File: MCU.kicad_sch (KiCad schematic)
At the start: 2 parts, among them U3 STM32L476RGTx, U4 ESP-12F

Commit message: Updates
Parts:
- added C10, C8, C9: 10u, Capacitor_SMD:C_0603_1608Metric_Pad1.08x0.95mm_HandSolder, symbol Device:C
- added C11: 10n, Capacitor_SMD:C_0603_1608Metric_Pad1.08x0.95mm_HandSolder, symbol Device:C
- added C12, C13: 1u, Capacitor_SMD:C_0603_1608Metric_Pad1.08x0.95mm_HandSolder, symbol Device:C
- added FB1: 120R, Inductor_SMD:L_0603_1608Metric_Pad1.05x0.95mm_HandSolder, symbol Device:FerriteBead
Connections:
- net +3.3V: now reaches U3.1 (VBAT)
- net +3.3V: now also U3.19 (VDD), U3.32 (VDD), U3.48 (VDDUSB), U3.64 (VDD), U4.8 (VCC), C10.1, C13.1, C8.1, C9.1, FB1.2
- net GND: now reaches U3.12 (VSSA)
- net GND: now also U3.18 (VSS), U3.31 (VSS), U3.47 (VSS), U3.63 (VSS), U4.15 (GND), C10.2, C11.2, C12.2, C13.2, C8.2, C9.2
- net +3.3VA: now reaches U3.13 (VDDA)
- net +3.3VA: now also C11.1, C12.1, FB1.1
- net ESP_RST: now reaches U4.1 (~{RST})
- net ESP_RXD: now reaches U4.21 (GPIO3/RXD)
- net ESP_TXD: now reaches U4.22 (GPIO1/TXD)
- net ESP_EN: now reaches U4.3 (EN)
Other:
- moved on the sheet: U3, U4

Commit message: Clock
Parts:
- added C14, C15, C16: 10u, Capacitor_SMD:C_0603_1608Metric_Pad1.08x0.95mm_HandSolder, symbol Device:C
- added R2: 10k, Resistor_SMD:R_0603_1608Metric_Pad0.98x0.95mm_HandSolder, symbol Device:R
- added Y1: 16MHz, Crystal:Crystal_SMD_3225-4Pin_3.2x2.5mm_HandSoldering, symbol Device:Crystal_GND24
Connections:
- net GND: now also C14.2, C15.2, C16.2, R2.1, Y1.2, Y1.4
- net CLK_IN: now reaches U3.5 (PH0)
- net CLK_IN: now also C15.1, Y1.1
- net CLK_OUT: now reaches U3.6 (PH1)
- net CLK_OUT: now also C16.1, Y1.3
- net at U3.60 (BOOT0): now also R2.2
- net at U3.7 (NRST): now also C14.1
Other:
- moved on the sheet: C10, C11, C12, C13, C8, C9, FB1

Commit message: uPDATE
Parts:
- added J2: SWD, Connector_PinHeader_1.00mm:PinHeader_1x03_P1.00mm_Vertical, symbol Connector_Generic:Conn_01x03
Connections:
- net ESP_EN: now also U3.3 (PC14)
- net ESP_RST: now also U3.4 (PC15)
- net ESP_RXD: now also U3.51 (PC10)
- net ESP_TXD: now also U3.52 (PC11)
- net GND: now also U4.18 (GPIO0), J2.1 (Pin_1)
- net SWDIO: now reaches U3.46 (PA13)
- net SWDIO: now also J2.2 (Pin_2)
- net SWDCLK: now reaches U3.49 (PA14)
- net SWDCLK: now also J2.3 (Pin_3)

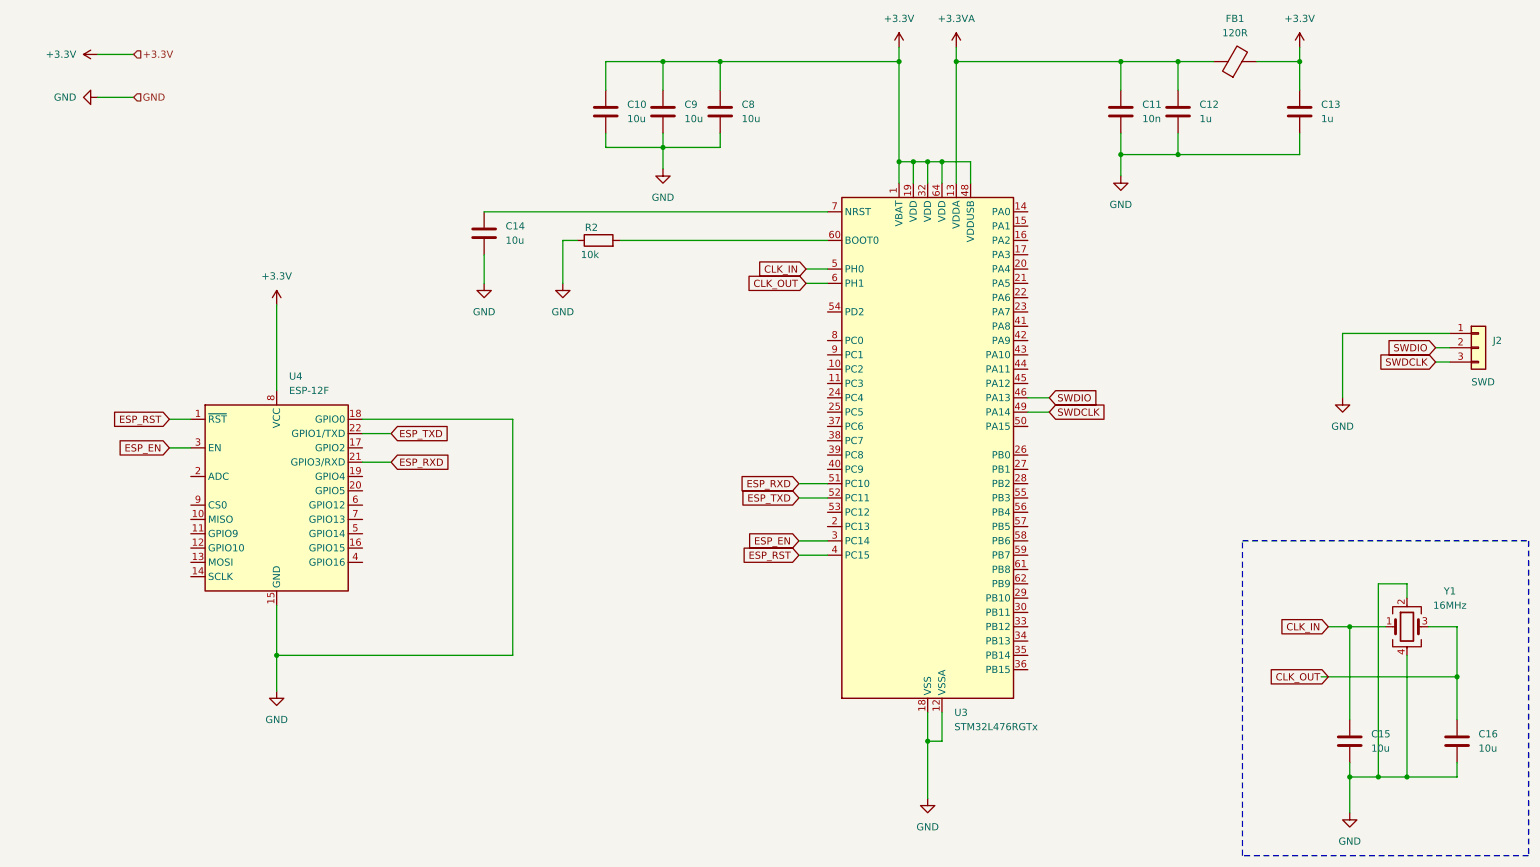
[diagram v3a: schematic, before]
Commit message: Schematic done
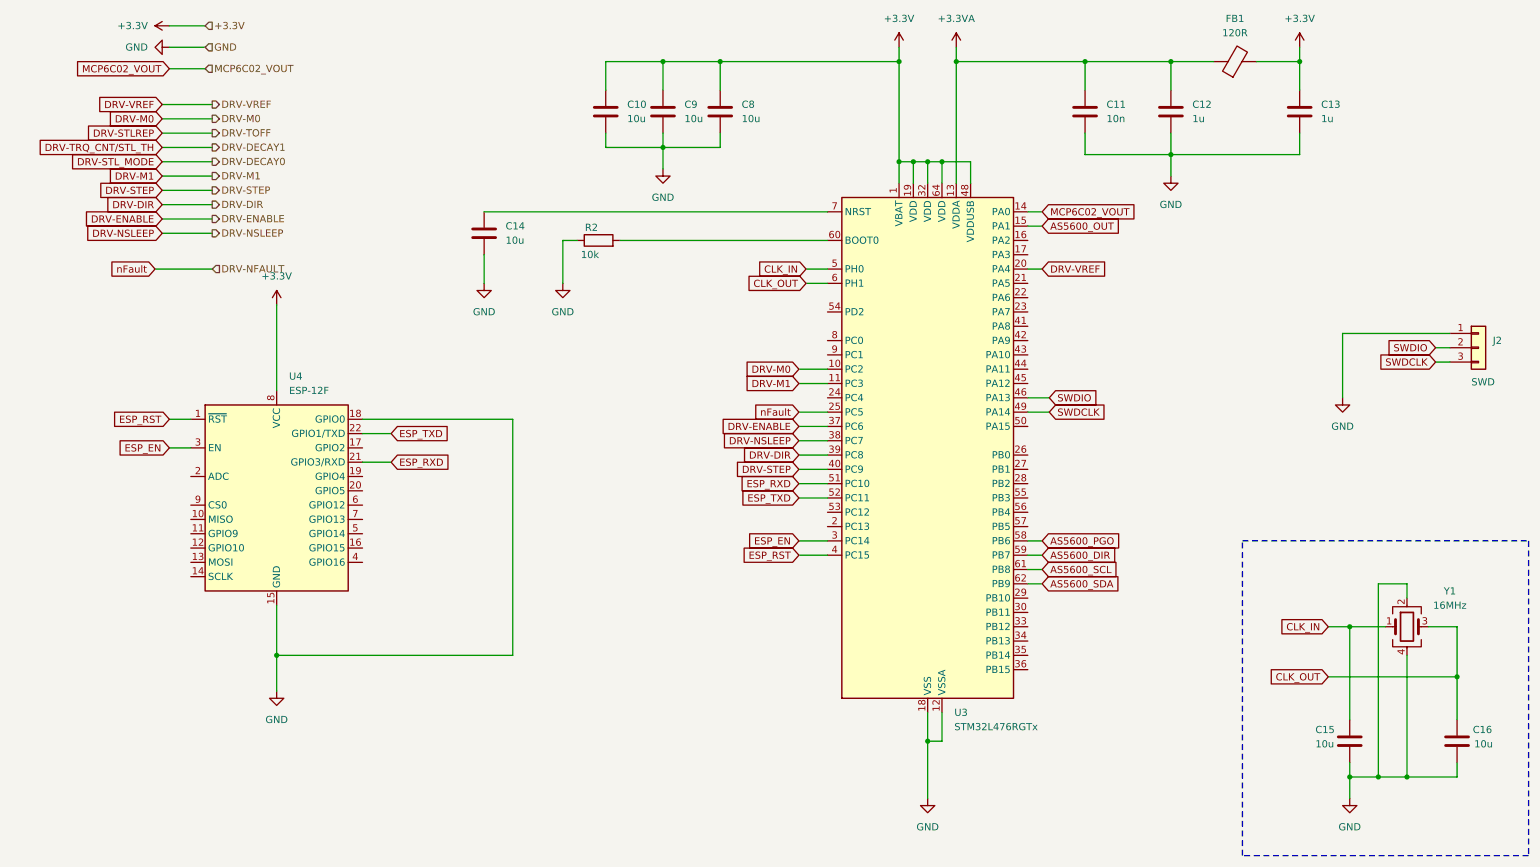
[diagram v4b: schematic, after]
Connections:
- net DRV-M0: now reaches U3.10 (PC2)
- net DRV-M1: now reaches U3.11 (PC3)
- net MCP6C02_VOUT: now reaches U3.14 (PA0)
- net AS5600_OUT: now reaches U3.15 (PA1)
- net DRV-VREF: now reaches U3.20 (PA4)
- net nFault: now reaches U3.25 (PC5)
- net DRV-ENABLE: now reaches U3.37 (PC6)
- net DRV-NSLEEP: now reaches U3.38 (PC7)
- net DRV-DIR: now reaches U3.39 (PC8)
- net DRV-STEP: now reaches U3.40 (PC9)
- net AS5600_PGO: now reaches U3.58 (PB6)
- net AS5600_DIR: now reaches U3.59 (PB7)
- net AS5600_SCL: now reaches U3.61 (PB8)
- net AS5600_SDA: now reaches U3.62 (PB9)
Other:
- moved on the sheet: C11, C12
